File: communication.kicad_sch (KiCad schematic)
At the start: 68 parts, among them J11 6x2.54mm, J12 6x2.54mm, J13 6x2.54mm, J14 6x2.54mm, J15 6x2.54mm, J16 6x2.54mm, Q26 BSS138, Q27 BSS138, Q28 BSS138, Q29 BSS138, Q30 BSS138, Q31 BSS138, Q32 BSS138, Q33 BSS138, Q34 BSS138, Q35 BSS138, Q36 BSS138, Q37 BSS138

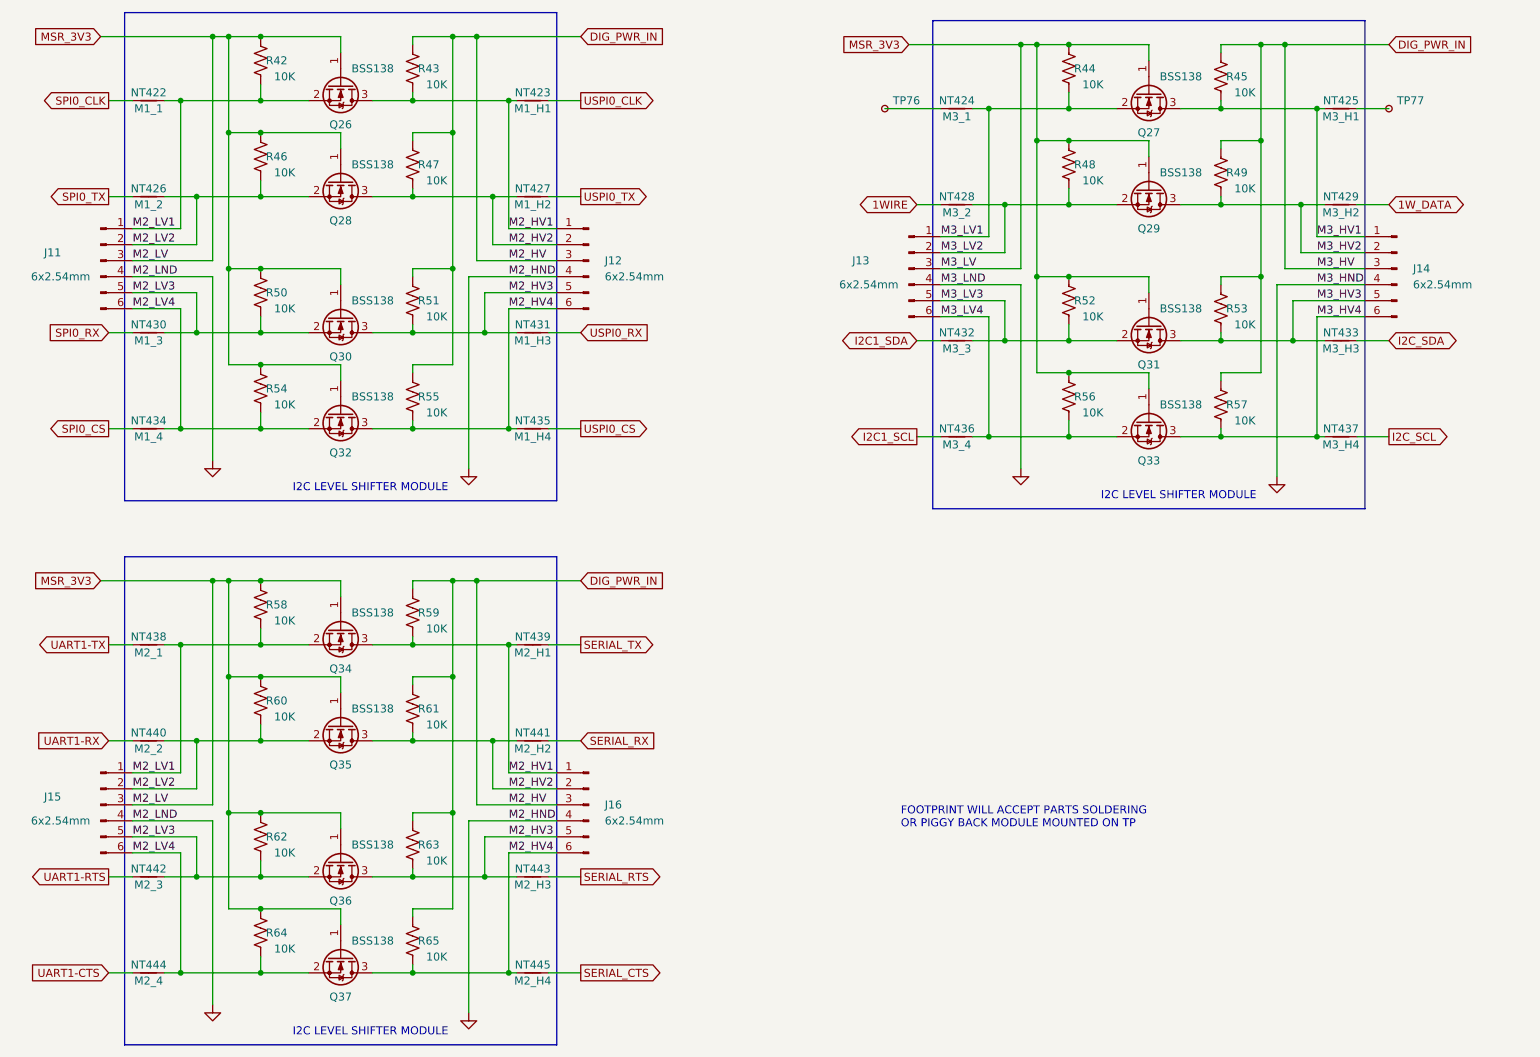
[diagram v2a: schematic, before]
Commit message: PCB Completed
PCB completed but final verification not completed
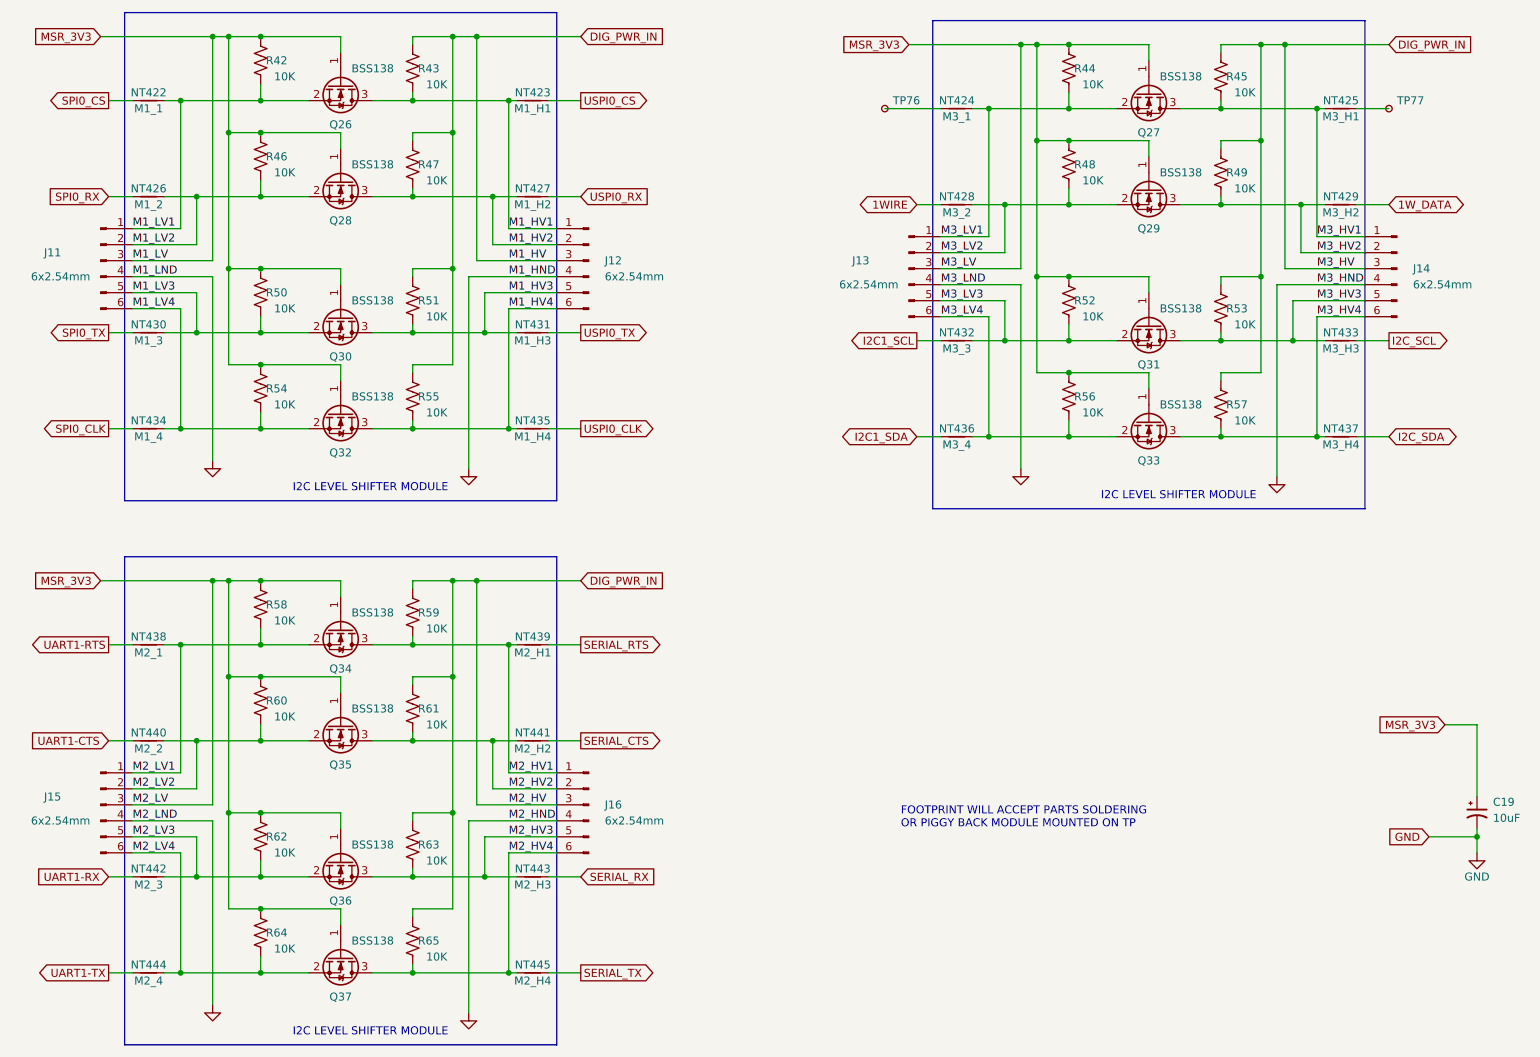
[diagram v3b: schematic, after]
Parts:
- added C19: 10uF, Capacitor_THT:CP_Radial_D4.0mm_P1.50mm, symbol Device:C_Polarized_Small_US
- J11, J12, J13, J14, J15, J16: footprint Connector_PinHeader_2.54mm:PinHeader_1x06_P2.54mm_Vertical -> Connector_PinSocket_2.54mm:PinSocket_1x06_P2.54mm_Vertical
- Q26, Q27, Q28, Q29, Q30, Q31, Q32, Q33, Q34, Q35, Q36, Q37: footprint Package_TO_SOT_SMD:SOT-23W -> Import_library:SOT-23W_SHORT
- TP76, TP77: footprint Connector_Pin:Pin_D0.9mm_L10.0mm_W2.4mm_FlatFork -> TestPoint:TestPoint_THTPad_D1.5mm_Drill0.7mm
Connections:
- net GND: now also C19.2
- net I2C1_SCL: now also NT432.1; no longer NT436.1
- net I2C1_SDA: now also NT436.1; no longer NT432.1
- net I2C_SCL: now also NT433.1; no longer NT437.1
- net I2C_SDA: now also NT437.1; no longer NT433.1
- net M2_HV1: no longer J12.1 (Pin_1), NT423.2, Q26.3 (D), R43.1
- net M2_HV2: no longer J12.2 (Pin_2), NT427.2, Q28.3 (D), R47.1
- net M2_HV3: no longer J12.5 (Pin_5), NT431.2, Q30.3 (D), R51.1
- net M2_HV4: no longer J12.6 (Pin_6), NT435.2, Q32.3 (D), R55.1
- net M2_LV1: no longer J11.1 (Pin_1), NT422.2, Q26.2 (S), R42.1
- net M2_LV2: no longer J11.2 (Pin_2), NT426.2, Q28.2 (S), R46.1
- net M2_LV3: no longer J11.5 (Pin_5), NT430.2, Q30.2 (S), R50.1
- net M2_LV4: no longer J11.6 (Pin_6), NT434.2, Q32.2 (S), R54.1
- net MSR_3V3: now also C19.1
- net SERIAL_CTS: now also NT441.1; no longer NT445.1
- net SERIAL_RTS: now also NT439.1; no longer NT443.1
- net SERIAL_RX: now also NT443.1; no longer NT441.1
- net SERIAL_TX: now also NT445.1; no longer NT439.1
- net SPI0_CLK: now also NT434.1; no longer NT422.1
- net SPI0_CS: now also NT422.1; no longer NT434.1
- net SPI0_RX: now also NT426.1; no longer NT430.1
- net SPI0_TX: now also NT430.1; no longer NT426.1
- net UART1-CTS: now also NT440.1; no longer NT444.1
- net UART1-RTS: now also NT438.1; no longer NT442.1
- net UART1-RX: now also NT442.1; no longer NT440.1
- net UART1-TX: now also NT444.1; no longer NT438.1
- net USPI0_CLK: now also NT435.1; no longer NT423.1
- net USPI0_CS: now also NT423.1; no longer NT435.1
- net USPI0_RX: now also NT427.1; no longer NT431.1
- net USPI0_TX: now also NT431.1; no longer NT427.1
- new net M1_HV1: J12.1 (Pin_1), NT423.2, Q26.3 (D), R43.1
- new net M1_HV2: J12.2 (Pin_2), NT427.2, Q28.3 (D), R47.1
- new net M1_HV3: J12.5 (Pin_5), NT431.2, Q30.3 (D), R51.1
- new net M1_HV4: J12.6 (Pin_6), NT435.2, Q32.3 (D), R55.1
- new net M1_LV1: J11.1 (Pin_1), NT422.2, Q26.2 (S), R42.1
- new net M1_LV2: J11.2 (Pin_2), NT426.2, Q28.2 (S), R46.1
- new net M1_LV3: J11.5 (Pin_5), NT430.2, Q30.2 (S), R50.1
- new net M1_LV4: J11.6 (Pin_6), NT434.2, Q32.2 (S), R54.1
